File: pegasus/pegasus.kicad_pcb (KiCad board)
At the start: 2 copper layers, 39 x 104.5 mm, 21 parts, among them IC2 RFD900, J1 Screw_Terminal_01x04, J2 Screw_Terminal_01x02, Q1 ST3413A, U1 Teensy4.0, U2 CON-SMA-EDGE-S, U3 CON-SMA-EDGE-S, U4 XTSD04GCLGEGA, U5 HT7350-A

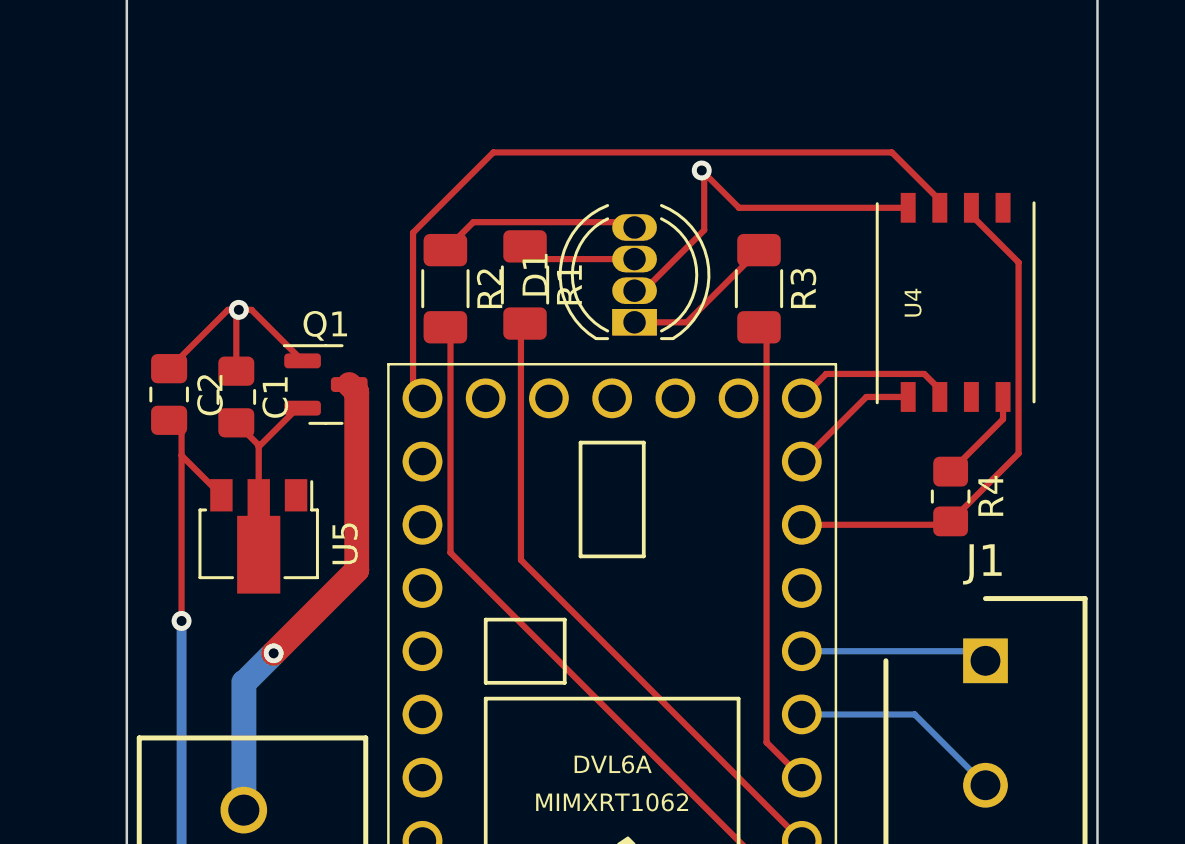
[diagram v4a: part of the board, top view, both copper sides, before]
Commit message: Voltage regulator fixes
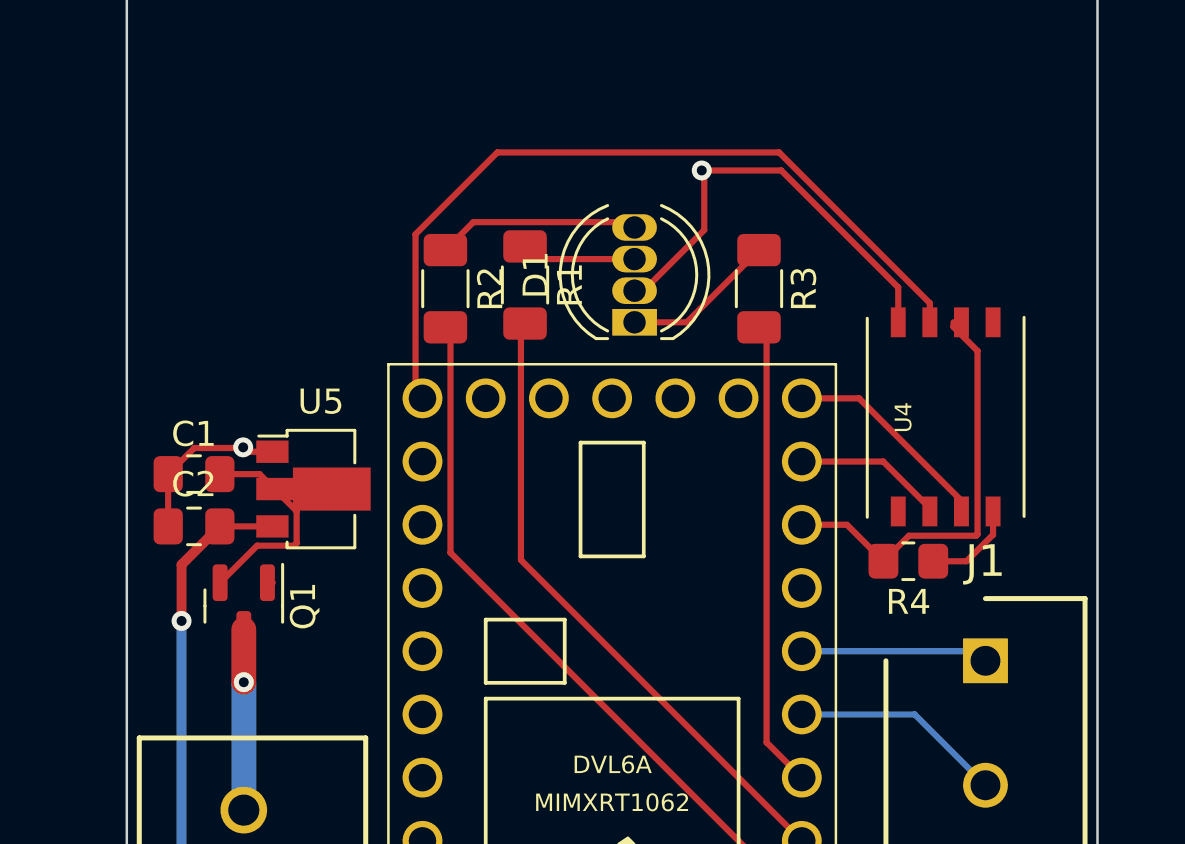
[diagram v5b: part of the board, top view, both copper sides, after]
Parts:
- moved Q1 9.49 mm to (90.7, 132.3), turned to -90 degrees
- moved C2 5.39 mm to (88.7, 129.1), turned to 0 degrees
- moved U4 4.62 mm to (118.9, 124.7)
- moved C1 3.54 mm to (88.7, 127.0), turned to 0 degrees
- moved R4 3.11 mm to (117.4, 130.5), turned to 180 degrees
- moved U5 2.91 mm to (93.5, 127.6), turned to 0 degrees
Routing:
- net /BATT+: track 18.9 -> 7.26 mm
- net +5V: track 38.6 -> 34.6 mm
- net Net-(C1-Pad2): track 5.78 -> 8.72 mm
- net /CS: track 20.6 -> 18.1 mm
- net /MISO: track 6.51 -> 8.60 mm
- net /SCK: track 30.4 -> 32.0 mm
- net /MOSI: track 5.35 -> 6.11 mm

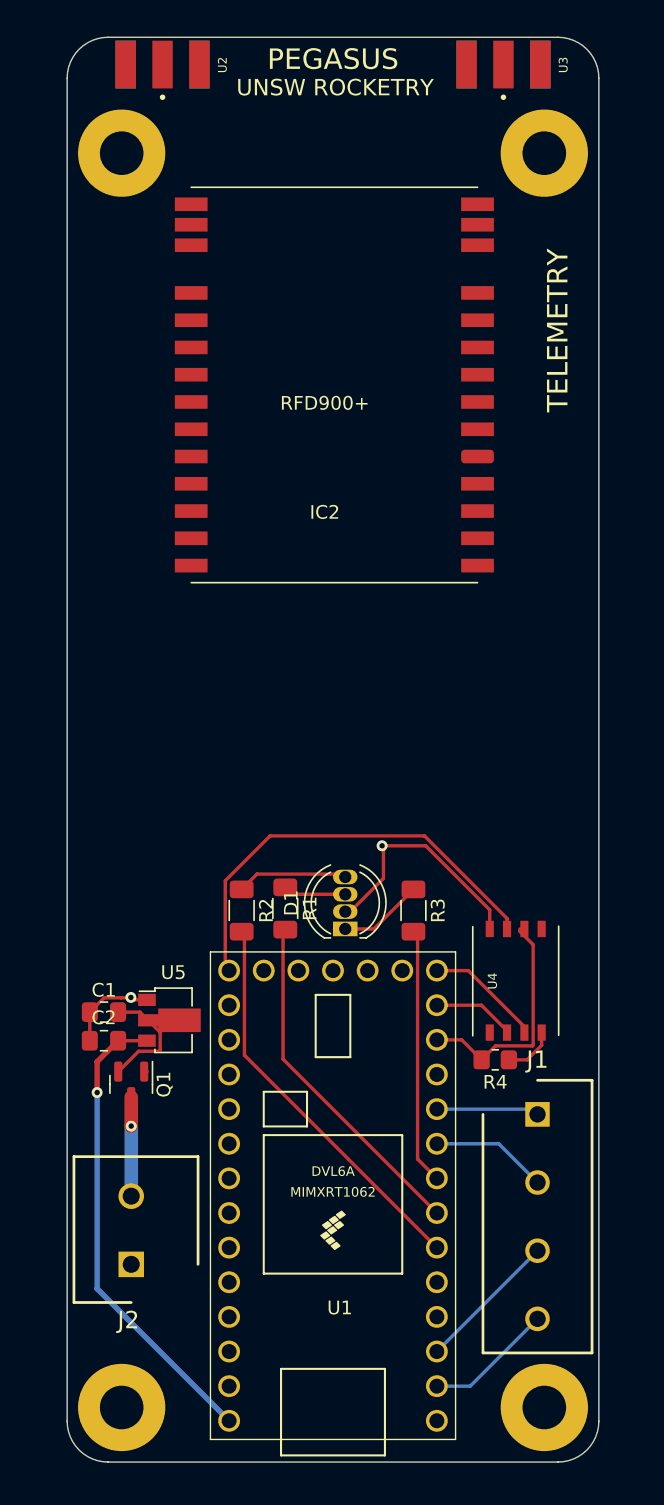
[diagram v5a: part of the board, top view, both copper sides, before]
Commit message: increasing spacing of components, route rx-tx of gps
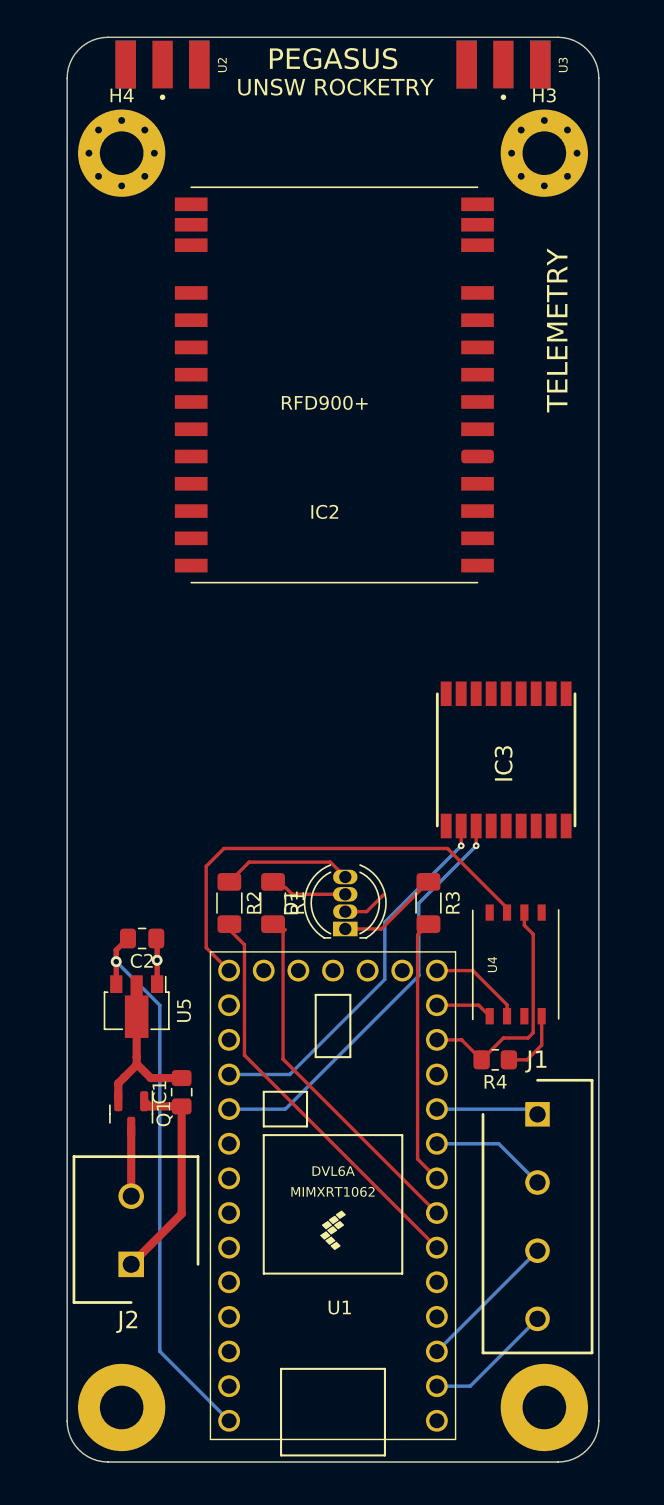
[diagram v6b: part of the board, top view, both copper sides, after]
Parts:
- added IC3: L70B-M39, Quectel_L70B-M39:1x18, F.Cu at (118.2, 108.5)
- H3, H4: footprint MountingHole:MountingHole_3.2mm_M3_Pad -> MountingHole:MountingHole_3.2mm_M3_Pad_Via
- moved C1 8.19 mm to (94.4, 132.9), turned to 90 degrees
- moved C2 8.01 mm to (91.5, 121.6), turned to 180 degrees
- moved U5 2.60 mm to (91.1, 126.6), turned to -90 degrees
- moved Q1 2.17 mm to (90.7, 134.5)
- moved R3 1.23 mm to (112.5, 119.0)
- moved U4 1.20 mm to (118.9, 123.5)
- moved R2 1.05 mm to (97.9, 119.0)
- moved R1 0.98 mm to (101.1, 119.0)
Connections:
- net Net-(IC2-Pad13) renamed /ANT1
- net Net-(IC2-Pad16) renamed /ANT2
- IC2 pad 12: Net-(IC2-Pad12) -> GND
- IC2 pad 14: Net-(IC2-Pad14) -> GND
- IC2 pad 15: Net-(IC2-Pad15) -> GND
- IC2 pad 17: Net-(IC2-Pad17) -> GND
- U2 pad G1: Net-(IC2-Pad15) -> GND
- U2 pad G2: Net-(IC2-Pad17) -> GND
- U3 pad G1: Net-(IC2-Pad12) -> GND
- U3 pad G2: Net-(IC2-Pad14) -> GND
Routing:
- net TX4: track 0.00 -> 30.7 mm, vias 0 -> 1
- net RX4: track 0.00 -> 27.9 mm, vias 0 -> 1
- net +5V: track 34.6 -> 40.8 mm
- net Net-(C1-Pad2): track 8.72 -> 12.8 mm
- net GND: track 24.7 -> 22.7 mm, vias 2 -> 1
- net /MISO: track 8.60 -> 6.68 mm
- net /MOSI: track 6.11 -> 4.21 mm
- net /BATT+: track 7.26 -> 5.66 mm, vias 1 -> 0
- net Net-(D1-Pad4): track 8.15 -> 9.55 mm
- net Net-(D1-Pad1): track 6.20 -> 7.53 mm
- net +3.3V: track 3.78 -> 4.98 mm
- net /SCK: track 32.0 -> 33.1 mm
- net RGB3: track 18.8 -> 19.6 mm
- net RGB1: track 29.1 -> 29.6 mm

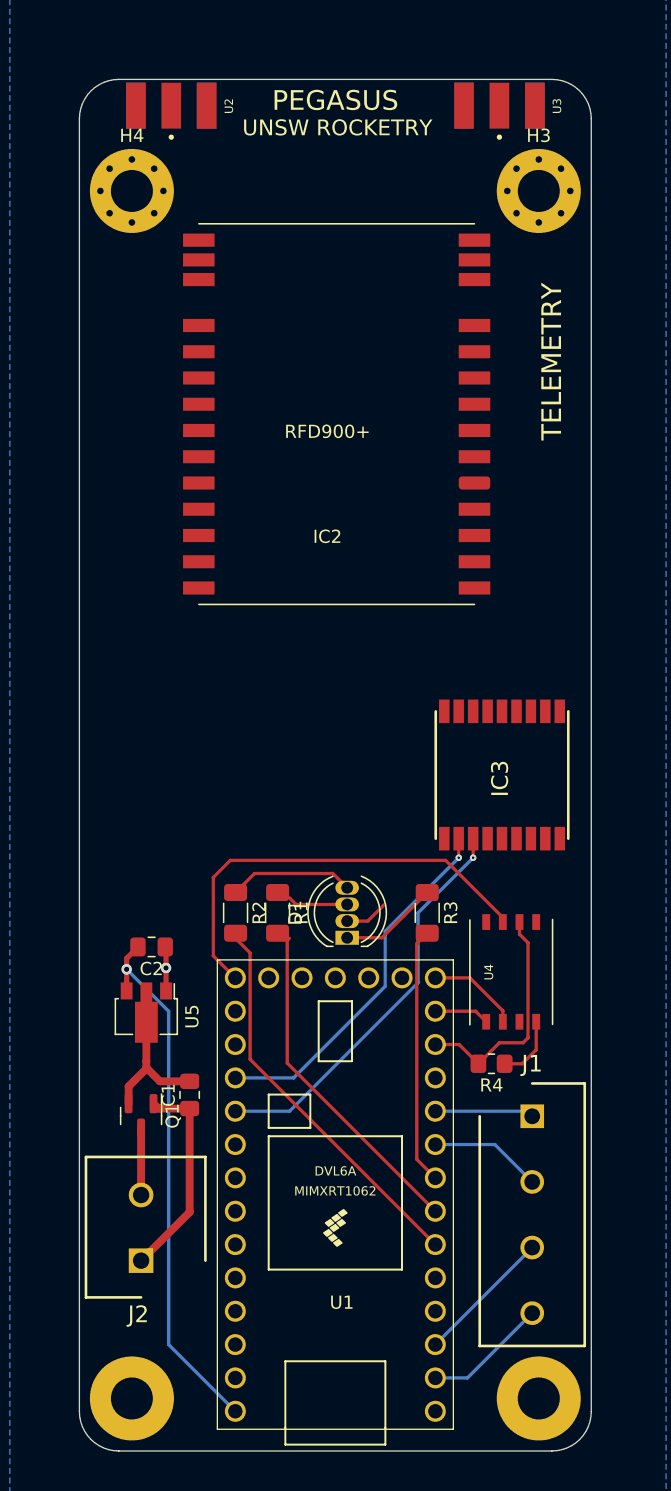
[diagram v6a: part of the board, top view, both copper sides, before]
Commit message: move rfd900 closer to gps, decrease length to 98mm
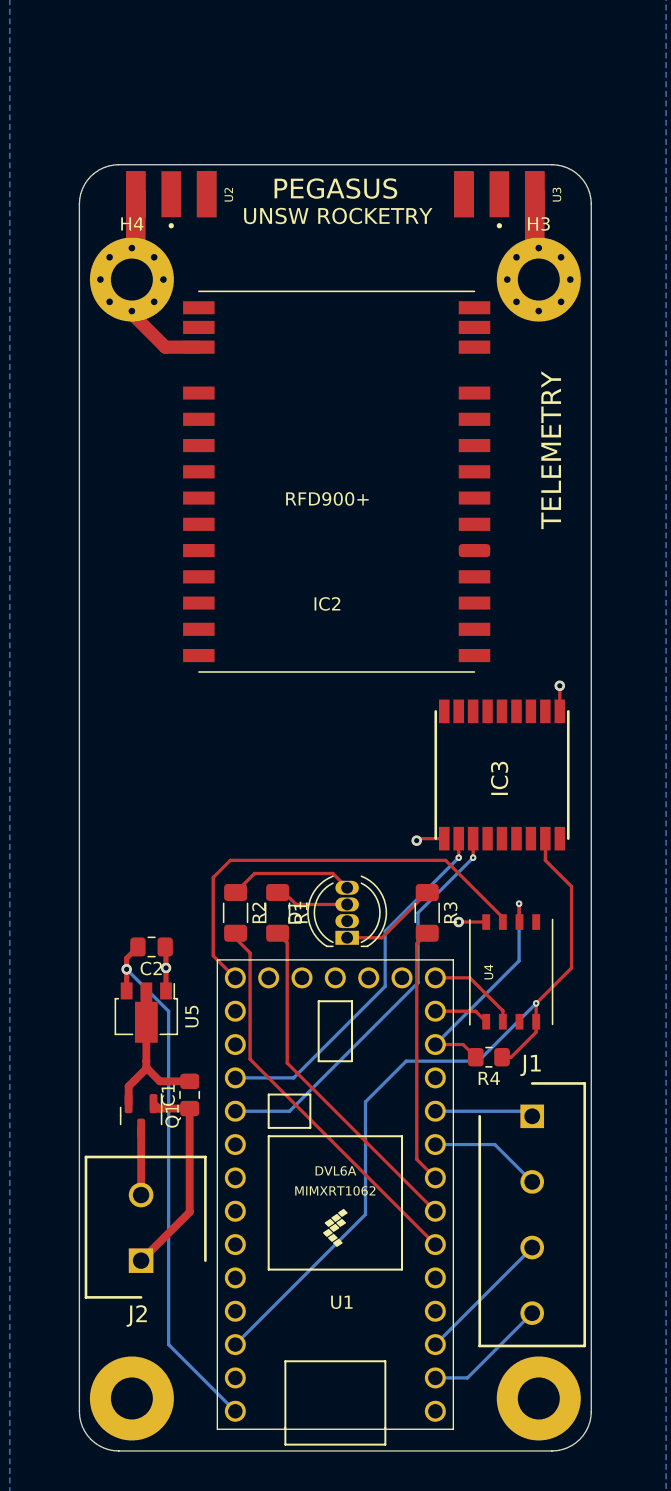
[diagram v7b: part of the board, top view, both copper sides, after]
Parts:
- moved G*** 6.75 mm to (105.5, 91.8)
- moved H3 6.75 mm to (121.0, 70.8)
- moved H4 6.75 mm to (90.0, 70.8)
- moved U2 6.75 mm to (93.0, 64.2)
- moved U3 6.75 mm to (118.0, 64.2)
- moved IC2 5.15 mm to (110.1, 89.4)
- moved R4 0.54 mm to (117.2, 130.0)
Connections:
- R4 pad 1: +3.3V -> 3.3V
- U4 pad 8: +3.3V -> 3.3V
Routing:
- net 3.3V: track 0.00 -> 58.8 mm, vias 0 -> 1
- net GND: track 22.7 -> 45.5 mm, vias 1 -> 4
- net +3.3V: track 4.98 -> 0.00 mm
- net /CS: track 18.3 -> 19.0 mm, vias 0 -> 1
- net RGB2: track 25.5 -> 26.2 mm
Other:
- board size 39 x 104.5 mm -> 39 x 98 mm

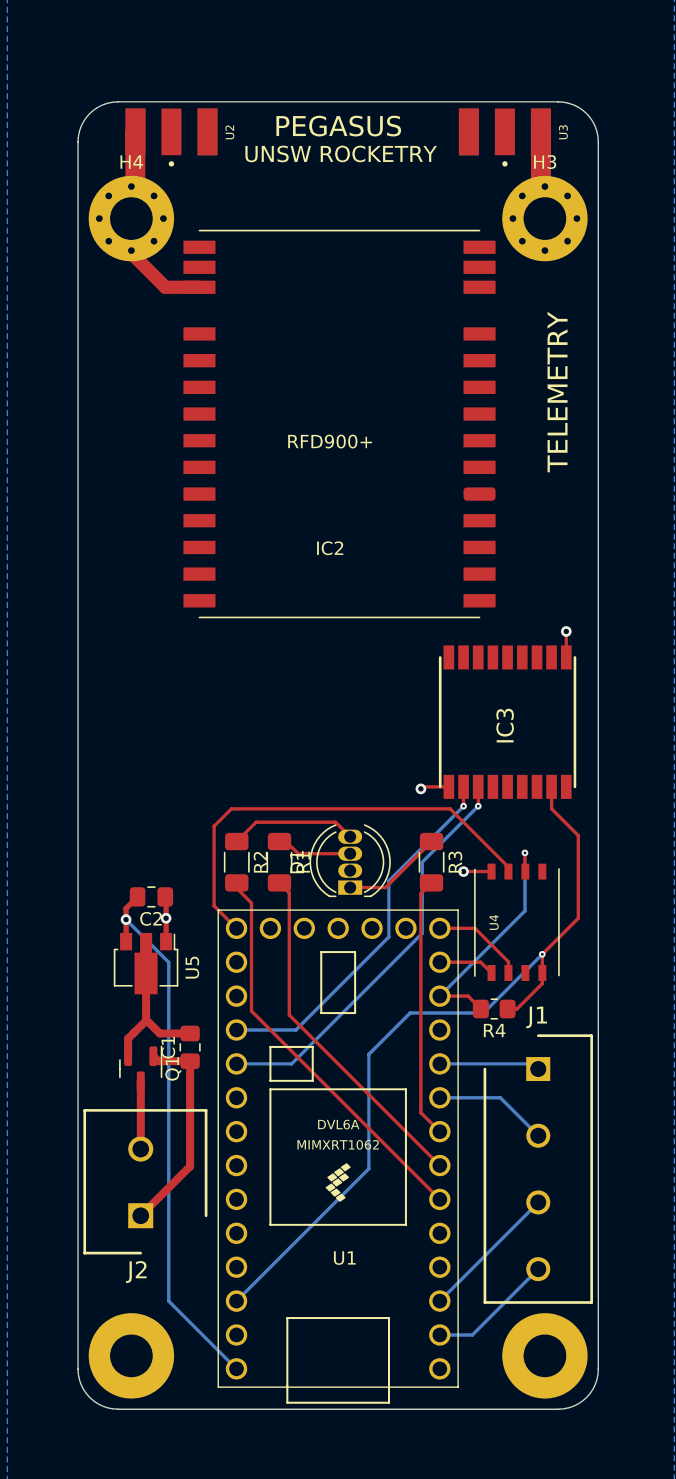
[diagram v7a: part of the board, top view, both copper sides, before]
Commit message: route all traces to rfd900
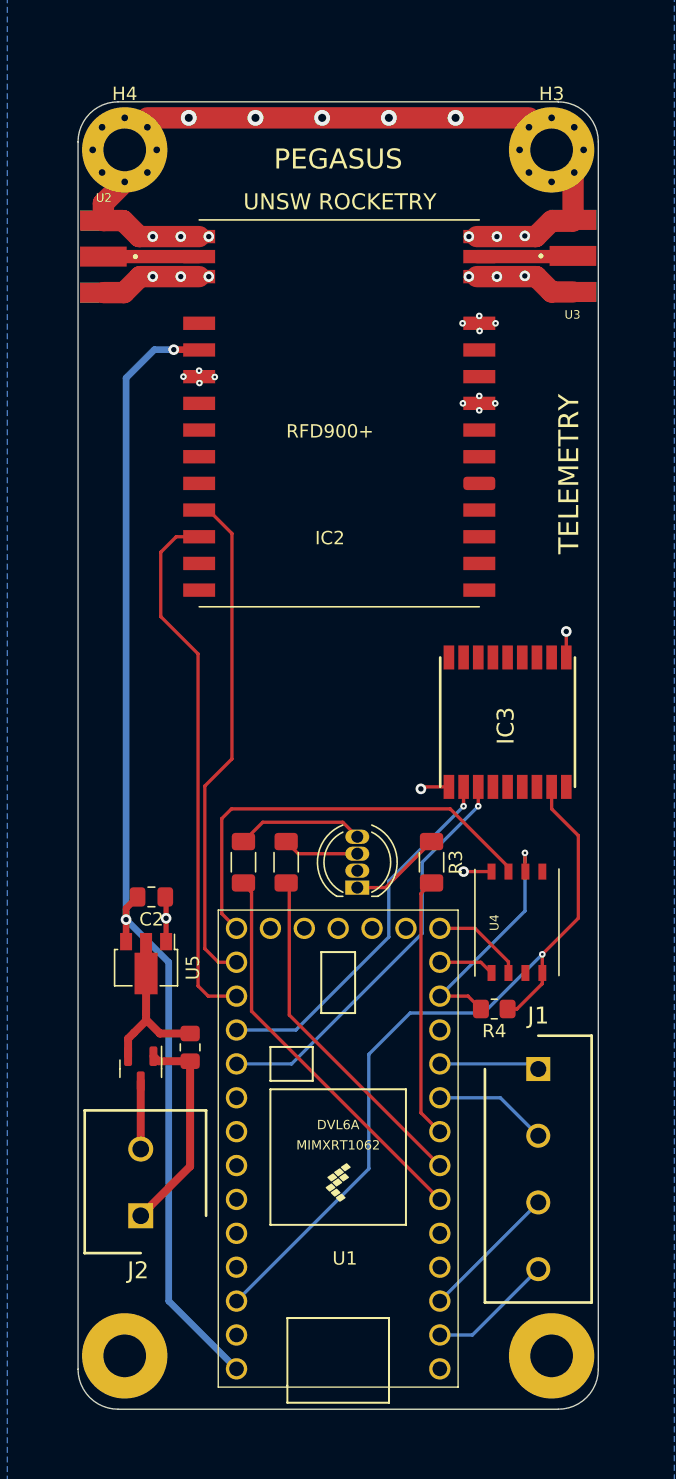
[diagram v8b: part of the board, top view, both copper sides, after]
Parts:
- moved U2 10.7 mm to (87.9, 73.6), turned to 0 degrees
- moved U3 10.6 mm to (123.1, 73.5), turned to 180 degrees
- moved H3 5.17 mm to (121.5, 65.6)
- moved H4 5.17 mm to (89.5, 65.6)
- moved G*** 3.75 mm to (105.5, 88.0)
- moved IC2 0.80 mm to (110.1, 88.6)
- moved D1 0.53 mm to (106.9, 120.9)
- moved H1 0.50 mm to (89.5, 156.0)
- moved H2 0.50 mm to (121.5, 156.0)
- moved R1 0.50 mm to (101.6, 119.0)
- moved R2 0.50 mm to (98.4, 119.0)
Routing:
- net GND: track 45.5 -> 94.5 mm, vias 4 -> 33
- net +5V: track 40.8 -> 87.9 mm, vias 1 -> 2
- net RX3: track 0.00 -> 40.2 mm
- net TX3: track 0.00 -> 37.9 mm
- net /ANT2: track 0.00 -> 7.18 mm
- net /ANT1: track 0.00 -> 7.18 mm
- net /CS: track 19.0 -> 18.3 mm
- net Net-(D1-Pad3): track 4.61 -> 5.18 mm
